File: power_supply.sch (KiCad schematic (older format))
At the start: 4 parts, among them U3 ST1S10PHR, U4 ST1S09IPUR

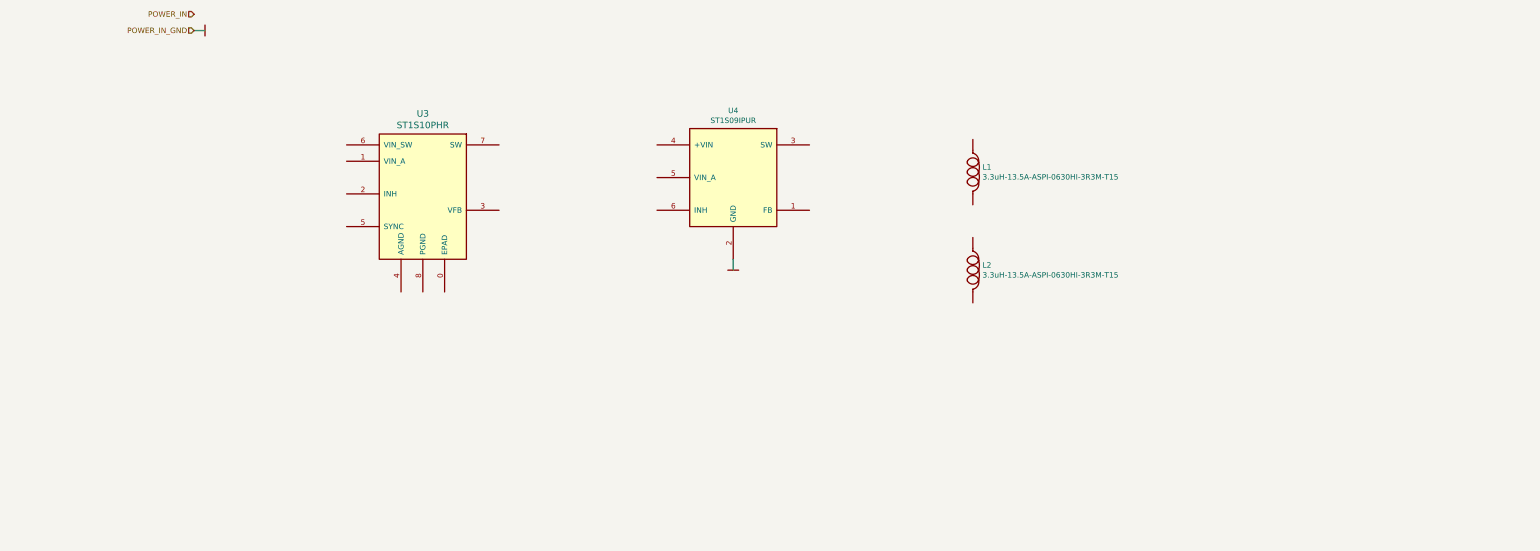
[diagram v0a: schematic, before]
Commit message: Added power source module
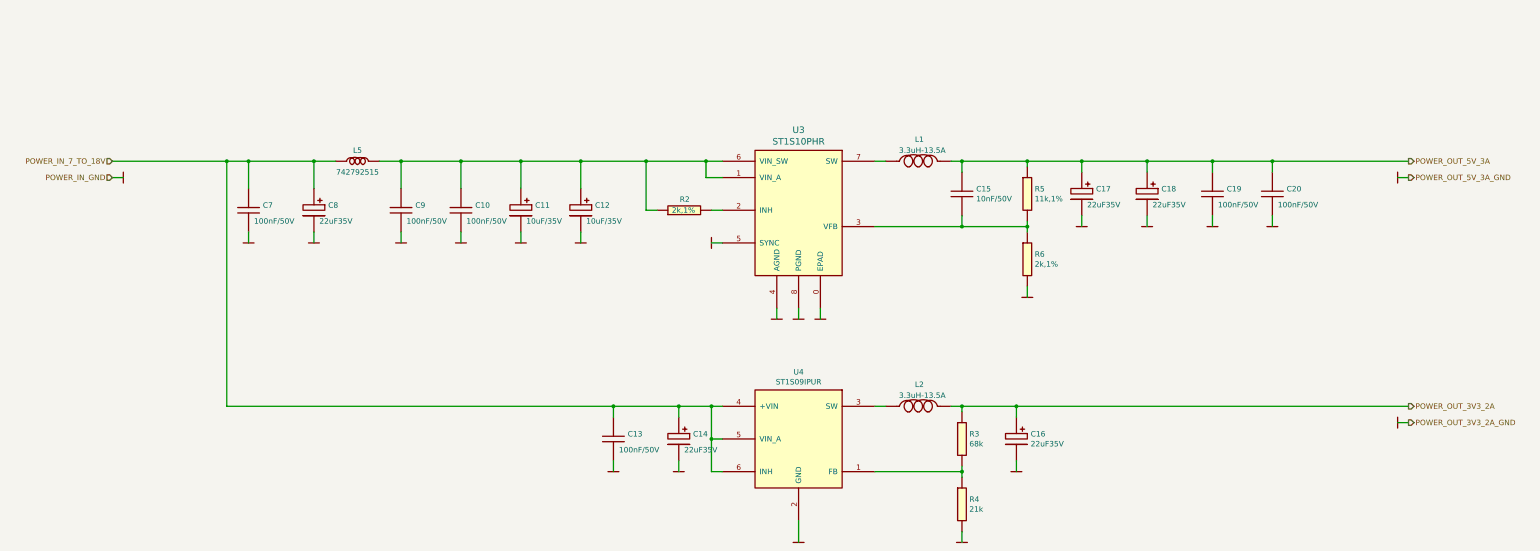
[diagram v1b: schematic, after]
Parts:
- added C10, C13, C19, C20, C7, C9: 100nF/50V, Capacitors_Smd_0603:100nF_0603, symbol Capacitors_Smd0603:100nF_0603
- added C11, C12: 10uF/35V, Smd_Tantal:10uF_35V_C, symbol Capacitors_Smd_Tantal:10uF_35V
- added C14, C16, C17, C18, C8: 22uF35V, Smd_Tantal:22uF_35V_Size_D, symbol Capacitors_Smd_Tantal:22uF35V
- added C15: 10nF/50V, Capacitors_Smd_0603:10nF_0603, symbol Capacitors_Smd0603:10nF_0603
- added L5: 742792515, Inductors:742792515, symbol Inductors:742792515
- added R2, R6: 2k,1%, Resistor_Smd_0603:2k_0603, symbol Resistors_Smd0603:2k
- added R3: 68k, Resistor_Smd_0603:68k_0603, symbol Resistors_Smd0603:68k
- added R4: 21k, Resistor_Smd_0603:21k_0603, symbol Resistors_Smd0603:21k
- added R5: 11k,1%, Resistor_Smd_0603:11k_0603, symbol Resistors_Smd0603:11k
- L1, L2: value 3.3uH-13.5A-ASPI-0630HI-3R3M-T15 -> 3.3uH-13.5A
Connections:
- net GND: now also U3.0 (EPAD), U3.4 (AGND), U3.5 (SYNC), U3.8 (PGND), C10.2, C11.2, C12.2, C13.2, C14.2, C16.2, C17.2, C18.2, C19.2, C20.2, C7.2, C8.2, C9.2, R4.2, R6.2
- net at U4.1 (FB): now also R3.2, R4.1
- net at U4.3 (SW): now also L2.1
- net POWER_IN_7_TO_18V: now reaches U4.4 (+VIN)
- net POWER_IN_7_TO_18V: now also U4.5 (VIN_A), U4.6 (INH), C13.1, C14.1, C7.1, C8.1, L5.1
- net at U3.1 (VIN_A): now also U3.6 (VIN_SW), C10.1, C11.1, C12.1, C9.1, L5.2, R2.1
- net at U3.2 (INH): now also R2.2
- net at U3.3 (VFB): now also C15.2, R5.2, R6.1
- net at U3.7 (SW): now also L1.1
- net POWER_OUT_5V_3A: now reaches L1.2
- net POWER_OUT_5V_3A: now also C15.1, C17.1, C18.1, C19.1, C20.1, R5.1
- net POWER_OUT_3V3_2A: now reaches L2.2
- net POWER_OUT_3V3_2A: now also C16.1, R3.1
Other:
- moved on the sheet: L1, L2, U3, U4

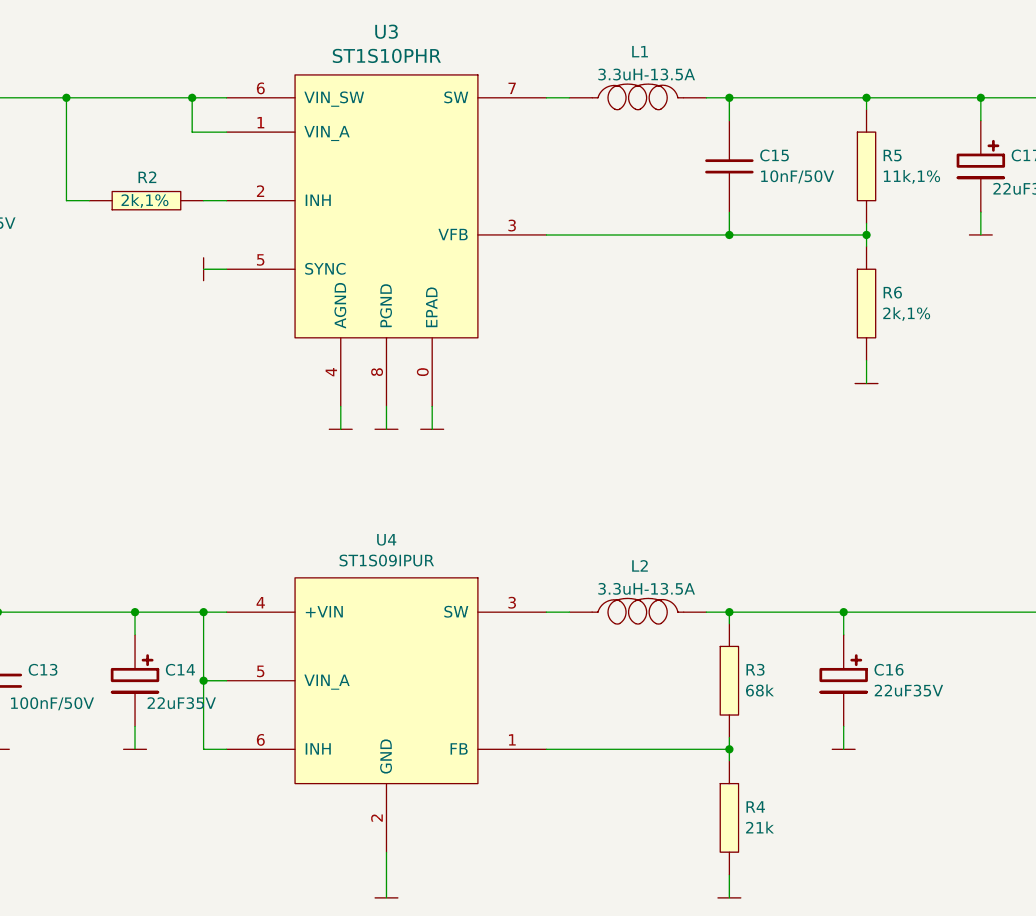
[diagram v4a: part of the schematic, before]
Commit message: Tracking finished, started tunning
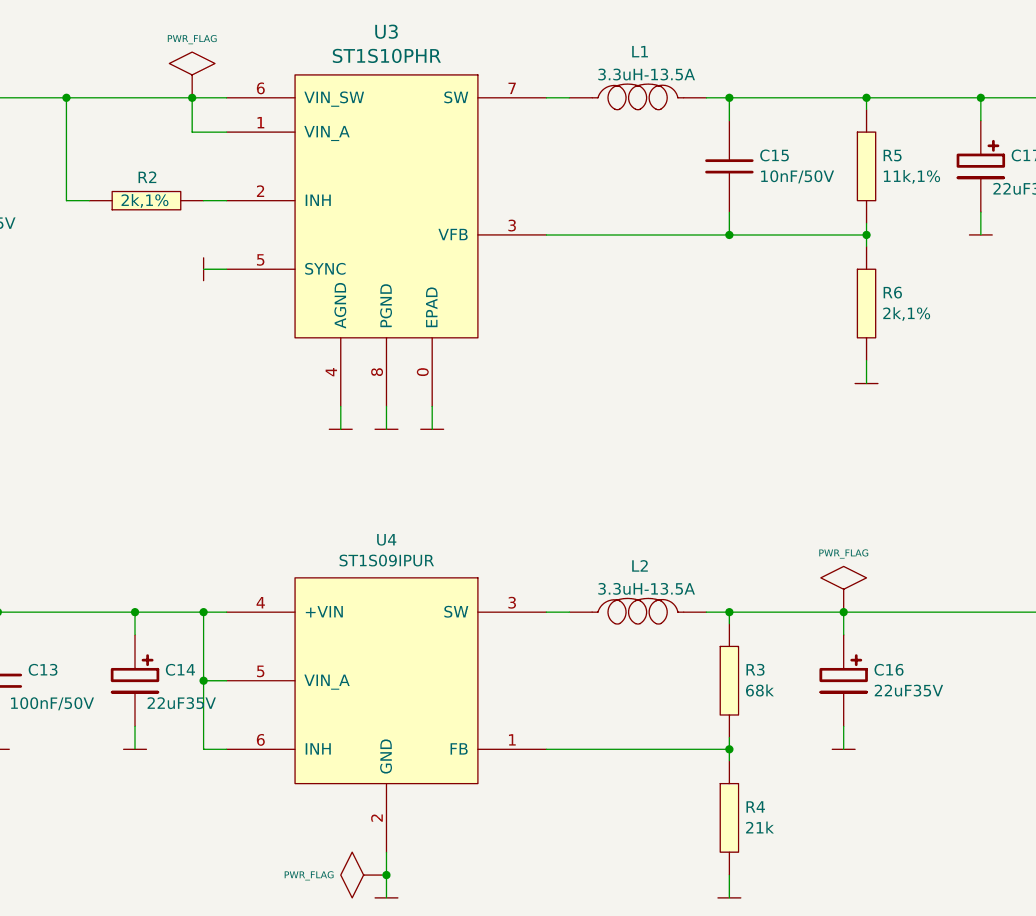
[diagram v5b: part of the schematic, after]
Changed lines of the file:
@@
 $EndComp
 Wire Wire Line
-	8400 7350 8400 7550
+	8400 7350 8400 7450
 Text HLabel 2100 4050 0    50   Input ~ 0
 POWER_IN_7_TO_18V
@@
 	2100 4050 3150 4050
 Connection ~ 3150 4050
+$Comp
+L power:PWR_FLAG #FLG0110
+U 1 1 60139248
+P 7550 4050
+F 0 "#FLG0110" H 7550 4320 30  0001 C CNN
+F 1 "PWR_FLAG" H 7550 4308 30  0000 C CNN
+F 2 "" H 7550 4050 60  0000 C CNN
+F 3 "" H 7550 4050 60  0000 C CNN
+	1    7550 4050
+	1    0    0    -1
+$EndComp
+$Comp
+L power:PWR_FLAG #FLG0101
+U 1 1 6026D9F2
+P 10400 6300
+F 0 "#FLG0101" H 10400 6570 30  0001 C CNN
+F 1 "PWR_FLAG" H 10400 6558 30  0000 C CNN
+F 2 "" H 10400 6300 60  0000 C CNN
+F 3 "" H 10400 6300 60  0000 C CNN
+	1    10400 6300
+	1    0    0    -1
+$EndComp
+$Comp
+L power:PWR_FLAG #FLG0102
+U 1 1 602710CA
+P 8400 7450
+F 0 "#FLG0102" H 8400 7720 30  0001 C CNN
+F 1 "PWR_FLAG" V 8400 7678 30  0000 L CNN
+F 2 "" H 8400 7450 60  0000 C CNN
+F 3 "" H 8400 7450 60  0000 C CNN
+	1    8400 7450
+	0    -1   -1   0
+$EndComp
+Connection ~ 8400 7450
+Wire Wire Line
+	8400 7450 8400 7550
 $EndSCHEMATC
